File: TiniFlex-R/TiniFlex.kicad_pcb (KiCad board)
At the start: 2 copper layers, 41 x 19 mm, 13 parts, among them J1 Conn_01x02, J2 USB_A, U1 ATtiny85-20SF

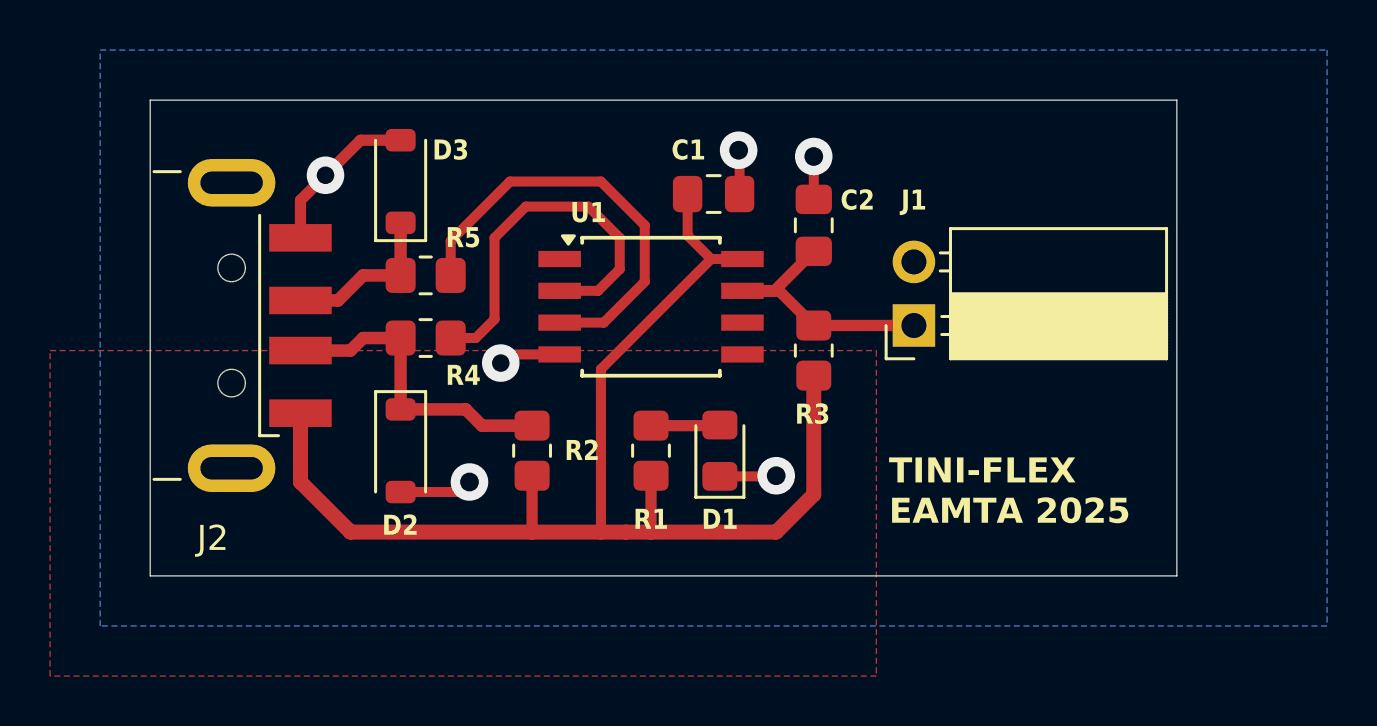
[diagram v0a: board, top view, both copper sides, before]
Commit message: Giro el integrado de TiniFlex-R
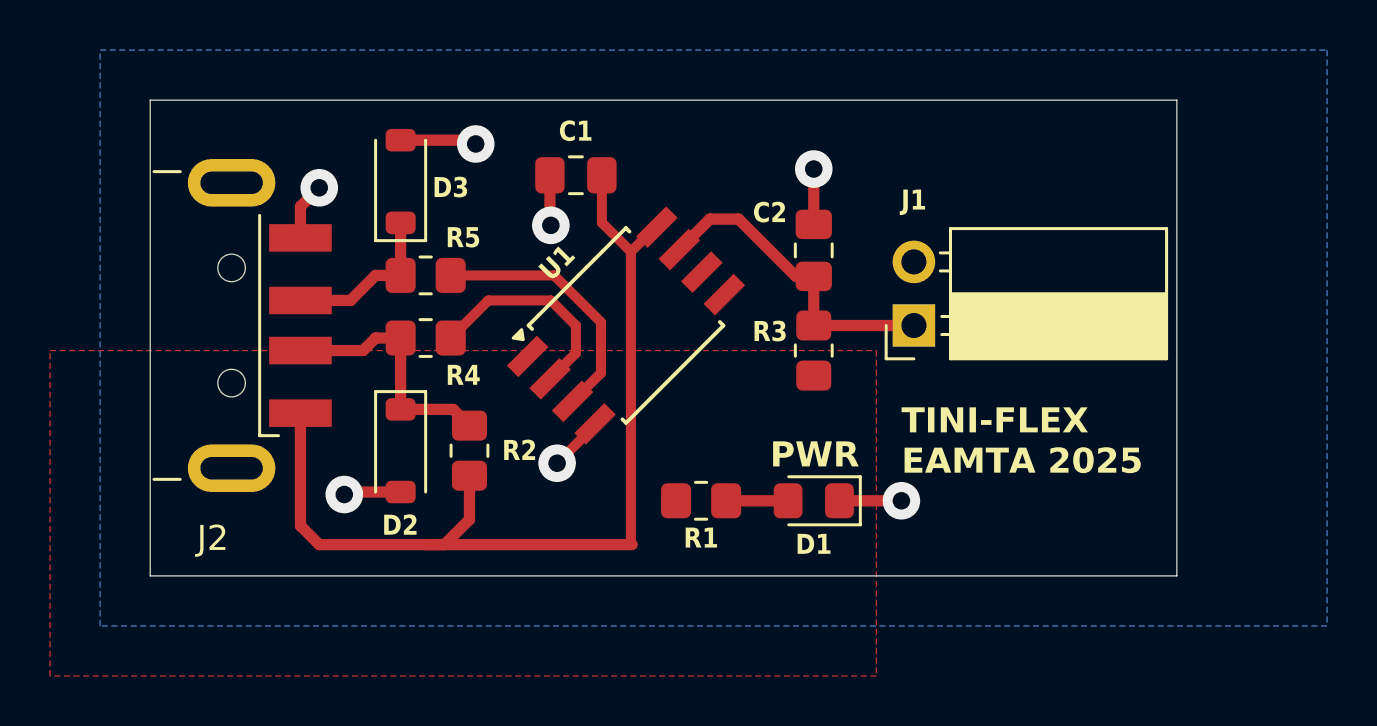
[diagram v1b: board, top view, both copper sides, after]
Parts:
- moved C1 5.55 mm to (196.0, 105.0), turned to 180 degrees
- moved D1 4.25 mm to (205.5, 118.0), turned to 180 degrees
- moved R1 2.83 mm to (201.0, 118.0), turned to 180 degrees
- moved R2 2.50 mm to (191.8, 116.0)
- moved U1 1.25 mm to (198.0, 111.0), turned to 45 degrees
- moved C2 1.00 mm to (205.5, 108.0)
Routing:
- net +5V: track 50.9 -> 38.7 mm
- net Net-(U1-XTAL1/PB3): track 15.4 -> 8.59 mm
- net Net-(U1-XTAL2/PB4): track 17.2 -> 10.4 mm
- net Net-(D2-K): track 12.6 -> 10.1 mm
- net Net-(J1-Pin_1): track 10.9 -> 12.8 mm
- net GND: track 17.6 -> 16.6 mm, vias 6 -> 7
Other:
- board text added: "PWR"
